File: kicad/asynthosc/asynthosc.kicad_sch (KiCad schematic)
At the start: 0 parts

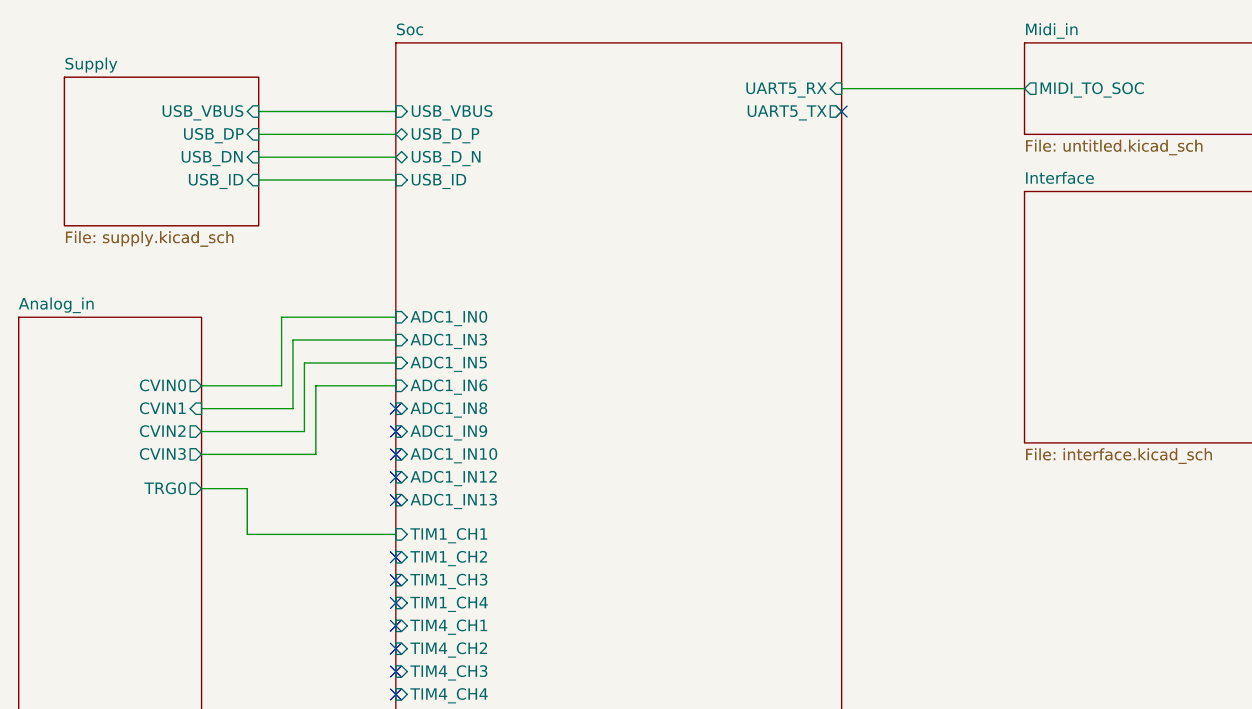
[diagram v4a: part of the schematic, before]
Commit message: sch: add spi nor, display connection, and more footprints
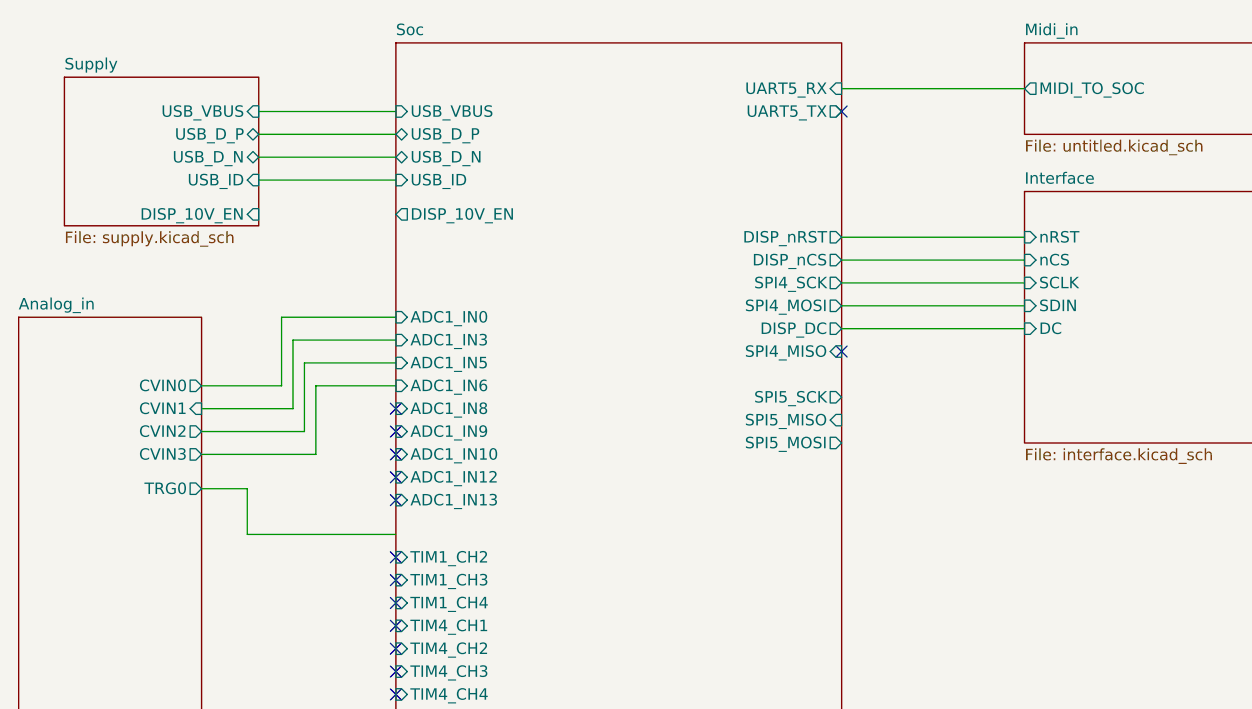
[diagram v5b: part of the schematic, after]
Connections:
- no-connect marks 13 -> 14
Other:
- sheet Interface ports: added DC, SCLK, SDIN, nCS, nRST; removed none
- sheet Soc ports: added DISP_10V_EN, DISP_DC, DISP_nCS, DISP_nRST, SPI4_MISO, SPI4_MOSI, SPI4_SCK, SPI5_MISO, SPI5_MOSI, SPI5_SCK; removed TIM1_CH1
- sheet Supply ports: added DISP_10V_EN, USB_D_N, USB_D_P; removed USB_DN, USB_DP
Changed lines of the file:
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@@
+	)
+	(no_connect
+		(at 176.53 105.41)
 	)
 	(no_connect
@@
 	(wire
 		(pts
+			(xy 176.53 102.87) (xy 196.85 102.87)
+		)
+		(stroke
+			(width 0)
+			(type default)
+		)
+	)
+	(wire
+		(pts
 			(xy 110.49 125.73) (xy 127 125.73)
 		)
@@
 	(wire
 		(pts
+			(xy 176.53 97.79) (xy 196.85 97.79)
+		)
+		(stroke
+			(width 0)
+			(type default)
+		)
+	)
+	(wire
+		(pts
 			(xy 176.53 76.2) (xy 196.85 76.2)
 		)
@@
 	(wire
 		(pts
+			(xy 176.53 100.33) (xy 196.85 100.33)
+		)
+		(stroke
+			(width 0)
+			(type default)
+		)
+	)
+	(wire
+		(pts
 			(xy 115.57 111.76) (xy 115.57 104.14)
 		)
@@
 	(wire
 		(pts
+			(xy 176.53 92.71) (xy 196.85 92.71)
+		)
+		(stroke
+			(width 0)
+			(type default)
+		)
+	)
+	(wire
+		(pts
 			(xy 110.49 120.65) (xy 110.49 125.73)
 		)
@@
 		(pts
 			(xy 105.41 111.76) (xy 115.57 111.76)
+		)
+		(stroke
+			(width 0)
+			(type default)
+		)
+	)
+	(wire
+		(pts
+			(xy 176.53 95.25) (xy 196.85 95.25)
 		)
 		(stroke
@@
 			)
 		)
-		(pin "USB_DP" input
-			(at 111.76 81.28 0)
-			(effects
-				(font
-					(size 1.27 1.27)
-				)
-				(justify right)
-			)
-		)
-		(pin "USB_DN" input
-			(at 111.76 83.82 0)
-			(effects
-				(font
-					(size 1.27 1.27)
-				)
-				(justify right)
-			)
-		)
 		(pin "USB_VBUS" input
 			(at 111.76 78.74 0)
@@
 		(pin "USB_ID" input
 			(at 111.76 86.36 0)
+			(effects
+				(font
+					(size 1.27 1.27)
+				)
+				(justify right)
+			)
+		)
+		(pin "USB_D_P" bidirectional
+			(at 111.76 81.28 0)
+			(effects
+				(font
+					(size 1.27 1.27)
+				)
+				(justify right)
+			)
+		)
+		(pin "USB_D_N" bidirectional
+			(at 111.76 83.82 0)
+			(effects
+				(font
+					(size 1.27 1.27)
+				)
+				(justify right)
+			)
+		)
+		(pin "DISP_10V_EN" input
+			(at 111.76 90.17 0)
 			(effects
 				(font
@@
 			)
 		)
+		(pin "nRST" input
+			(at 196.85 92.71 180)
+			(effects
+				(font
+					(size 1.27 1.27)
+				)
+				(justify left)
+			)
+		)
+		(pin "DC" input
+			(at 196.85 102.87 180)
+			(effects
+				(font
+					(size 1.27 1.27)
+				)
+				(justify left)
+			)
+		)
+		(pin "nCS" input
+			(at 196.85 95.25 180)
+			(effects
+				(font
+					(size 1.27 1.27)
+				)
+				(justify left)
+			)
+		)
+		(pin "SCLK" input
+			(at 196.85 97.79 180)
+			(effects
+				(font
+					(size 1.27 1.27)
+				)
+				(justify left)
+			)
+		)
+		(pin "SDIN" input
+			(at 196.85 100.33 180)
+			(effects
+				(font
+					(size 1.27 1.27)
+				)
+				(justify left)
+			)
+		)
 		(instances
 			(project "asynthosc"
@@
 			)
 		)
-		(pin "TIM1_CH1" input
-			(at 127 125.73 180)
-			(effects
-				(font
-					(size 1.27 1.27)
-				)
-				(justify left)
-			)
-		)
 		(pin "TIM1_CH2" input
 			(at 127 128.27 180)
@@
 			(effects
 				(font
+					(size 1.27 1.27)
+				)
+				(justify right)
+			)
+		)
+		(pin "DISP_10V_EN" output
+			(at 127 90.17 180)
+			(effects
+				(font
+					(size 1.27 1.27)
+				)
+				(justify left)
+			)
+		)
+		(pin "DISP_DC" output
+			(at 176.53 102.87 0)
+			(effects
+				(font
+					(size 1.27 1.27)
+				)
+				(justify right)
+			)
+		)
+		(pin "DISP_nRST" output
+			(at 176.53 92.71 0)
+			(effects
+				(font
+					(size 1.27 1.27)
+				)
+				(justify right)
+			)
+		)
+		(pin "SPI4_MOSI" output
+			(at 176.53 100.33 0)
+			(effects
+				(font
+					(size 1.27 1.27)
+				)
+				(justify right)
+			)
+		)
+		(pin "SPI4_SCK" output
+			(at 176.53 97.79 0)
+			(effects
+				(font
+					(size 1.27 1.27)
+				)
+				(justify right)
+			)
+		)
+		(pin "SPI4_MISO" input
+			(at 176.53 105.41 0)
+			(effects
+				(font
+					(size 1.27 1.27)
+				)
+				(justify right)
+			)
+		)
+		(pin "SPI5_SCK" output
+			(at 176.53 110.49 0)
+			(effects
+				(font
+					(size 1.27 1.27)
+				)
+				(justify right)
+			)
+		)
+		(pin "SPI5_MISO" input
+			(at 176.53 113.03 0)
+			(effects
+				(font
+					(size 1.27 1.27)
+				)
+				(justify right)
+			)
+		)
+		(pin "SPI5_MOSI" output
+			(at 176.53 115.57 0)
+			(effects
+				(font
+					(size 1.27 1.27)
+				)
+				(justify right)
+			)
+		)
+		(pin "DISP_nCS" output
+			(at 176.53 95.25 0)
+			(effects
+				(font

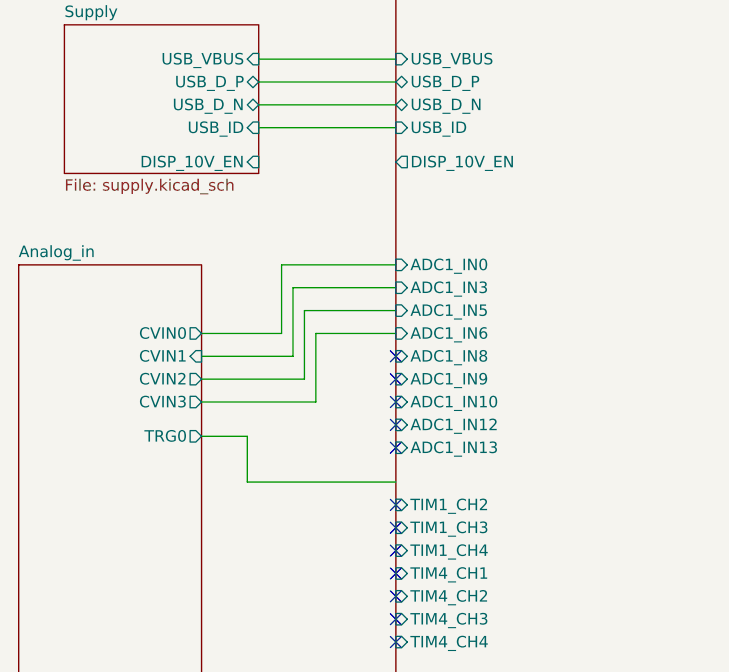
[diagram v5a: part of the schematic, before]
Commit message: sch: power supply improvements
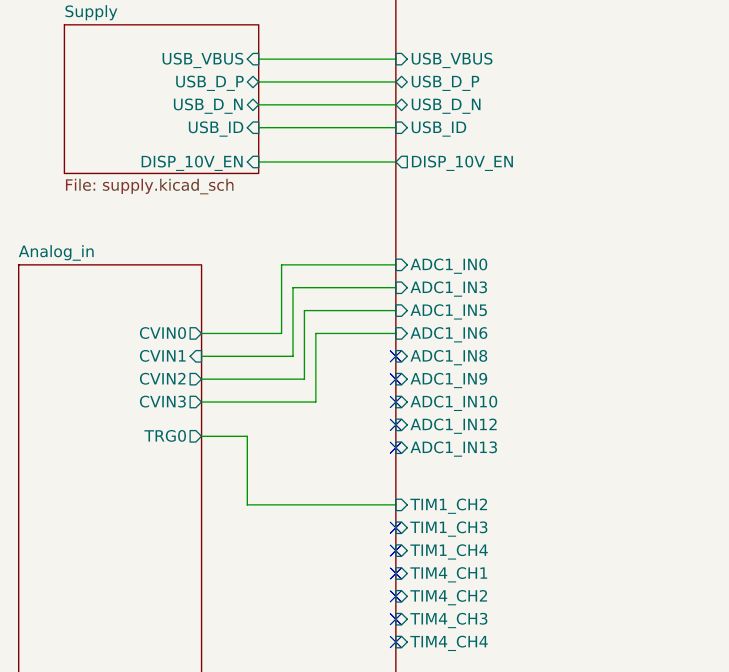
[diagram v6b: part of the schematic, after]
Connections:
- no-connect marks 14 -> 13
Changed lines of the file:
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@@
-	)
-	(no_connect
-		(at 127 128.27)
 	)
 	(no_connect
@@
 	(wire
 		(pts
-			(xy 110.49 125.73) (xy 127 125.73)
+			(xy 110.49 128.27) (xy 127 128.27)
 		)
 		(stroke
@@
 	(wire
 		(pts
+			(xy 111.76 90.17) (xy 127 90.17)
+		)
+		(stroke
+			(width 0)
+			(type default)
+		)
+	)
+	(wire
+		(pts
 			(xy 115.57 111.76) (xy 115.57 104.14)
 		)
@@
 	(wire
 		(pts
-			(xy 110.49 120.65) (xy 110.49 125.73)
+			(xy 110.49 120.65) (xy 110.49 128.27)
 		)
 		(stroke

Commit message: wip
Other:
- sheet Analog_in ports: added TRG1; removed none
- sheet Interface ports: added BTN_1, BTN_2, LED_BTN_1, LED_BTN_2, ROT_A, ROT_B; removed none
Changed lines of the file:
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@@
+	(wire
+		(pts
+			(xy 107.95 130.81) (xy 107.95 123.19)
+		)
+		(stroke
+			(width 0)
+			(type default)
+		)
+	)
 	(wire
 		(pts
@@
 	(wire
 		(pts
+			(xy 107.95 123.19) (xy 105.41 123.19)
+		)
+		(stroke
+			(width 0)
+			(type default)
+		)
+	)
+	(wire
+		(pts
 			(xy 105.41 114.3) (xy 116.84 114.3)
 		)
@@
 		(pts
 			(xy 105.41 151.13) (xy 127 151.13)
+		)
+		(stroke
+			(width 0)
+			(type default)
+		)
+	)
+	(wire
+		(pts
+			(xy 127 130.81) (xy 107.95 130.81)
 		)
 		(stroke
@@
 			)
 		)
+		(pin "TRG1" output
+			(at 105.41 123.19 0)
+			(effects
+				(font
+					(size 1.27 1.27)
+				)
+				(justify right)
+			)
+		)
 		(instances
 			(project "asynthosc"
@@
 	(sheet
 		(at 196.85 87.63)
-		(size 25.4 27.94)
+		(size 25.4 41.91)
 		(fields_autoplaced yes)
 		(stroke
@@
 		)
 		(property "Sheetfile" "interface.kicad_sch"
-			(at 196.85 116.1546 0)
+			(at 196.85 130.1246 0)
 			(effects
 				(font
@@
 			(effects
 				(font
+					(size 1.27 1.27)
+				)
+				(justify left)
+			)
+		)
+		(pin "ROT_B" output
+			(at 196.85 106.68 180)
+			(effects
+				(font
+					(size 1.27 1.27)
+				)
+				(justify left)
+			)
+		)
+		(pin "ROT_A" output
+			(at 196.85 109.22 180)
+			(effects
+				(font
+					(size 1.27 1.27)
+				)
+				(justify left)
+			)
+		)
+		(pin "BTN_1" output
+			(at 196.85 111.76 180)
+			(effects
+				(font
+					(size 1.27 1.27)
+				)
+				(justify left)
+			)
+		)
+		(pin "LED_BTN_1" input
+			(at 196.85 114.3 180)
+			(effects
+				(font
+					(size 1.27 1.27)
+				)
+				(justify left)
+			)
+		)
+		(pin "BTN_2" output
+			(at 196.85 116.84 180)
+			(effects
+				(font
+					(size 1.27 1.27)
+				)
+				(justify left)
+			)
+		)
+		(pin "LED_BTN_2" input
+			(at 196.85 119.38 180)
+			(effects
+				(font

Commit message: pcb: placing
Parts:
- added TP10, TP11, TP12, TP13, TP14, TP15, TP16, TP17, TP18, TP5, TP6, TP7, TP8, TP9: TestPoint, TestPoint:TestPoint_Pad_D1.0mm, symbol Connector:TestPoint
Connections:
- net Analog_in/CVIN0: now also TP10.1
- net Analog_in/CVIN1: now also TP11.1
- net Analog_in/CVIN2: now also TP12.1
- net Analog_in/CVIN3: now also TP13.1
- net Analog_in/LOUT: now also TP17.1
- net Analog_in/TRG0: now also TP14.1
- net Analog_in/TRG1: now also TP15.1
- net Interface/DC: now also TP9.1
- net Interface/SCLK: now also TP7.1
- net Interface/SDIN: now also TP8.1
- net Interface/nCS: now also TP6.1
- net Interface/nRST: now also TP5.1
- net Midi_in/MIDI_TO_SOC: now also TP18.1
- net Soc/DISP_10V_EN: now also TP16.1
